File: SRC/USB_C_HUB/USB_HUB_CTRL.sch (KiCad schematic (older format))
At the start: 48 parts, among them U10 USB7206, Y7 25MHz_402F2501XIAR

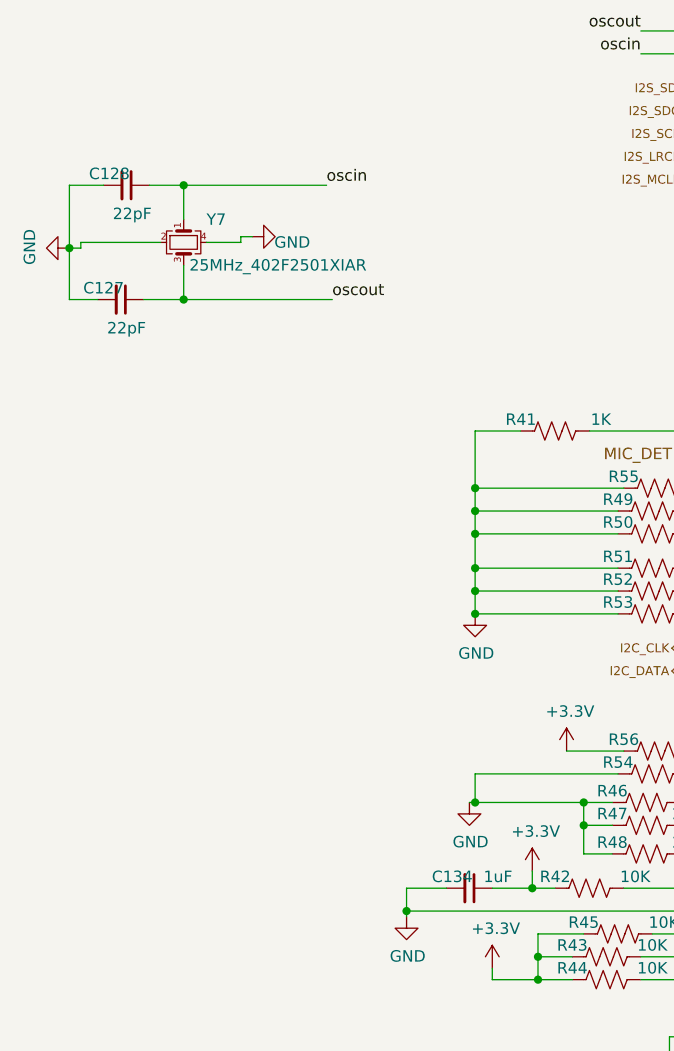
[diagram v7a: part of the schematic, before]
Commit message: schematic capture and footprint assignment complete. Pending approval
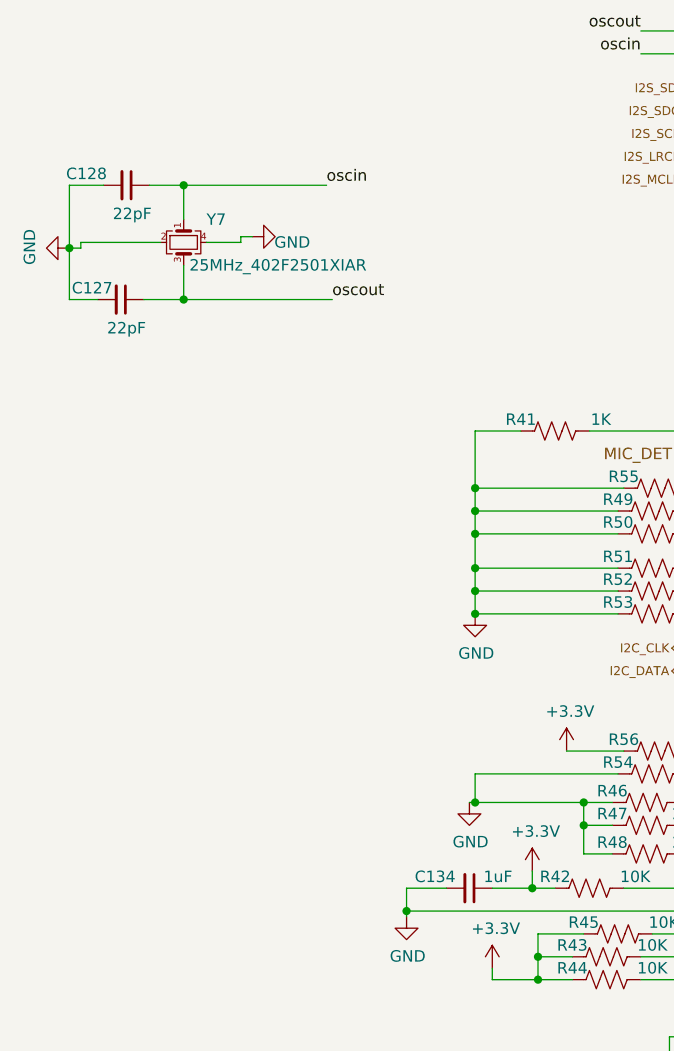
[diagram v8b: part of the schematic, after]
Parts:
- C127, C128: footprint (none) -> Capacitor_SMD:C_0402_1005Metric; Mfr No (none) -> CC0402JRNPO9BN220
- C129, C130, C131, C132, C133, C135, C136, C137, C138, C139, C140, C141, C142, C143, C144, C145, C146, C147, C148, C149, C150, C151, C152, C153, C154, C155: footprint (none) -> Capacitor_SMD:C_0402_1005Metric
- C134: footprint (none) -> Capacitor_SMD:C_0402_1005Metric; Mfr No (none) -> CL05A105KQ5NNNC
- R41, R42, R43, R44, R45, R46, R47, R48, R49, R50, R51, R52, R53, R54, R55, R56, R57: footprint (none) -> Resistor_SMD:R_0402_1005Metric
- U10: footprint (none) -> footprints:QFN40P1200X1200X90-101N
- Y7: footprint (none) -> Crystal:Crystal_SMD_2016-4Pin_2.0x1.6mm
